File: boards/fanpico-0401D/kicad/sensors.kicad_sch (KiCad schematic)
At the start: 22 parts, among them J1 Floppy Power Connector, J16 Sensor1, J17 Sensor2, J18 LCD (SPI), J19 Serial Console (TTL), J2 I2C (OLED ALT), J3 I2C (OLED), J5 1-Wire, J6 QWIIC

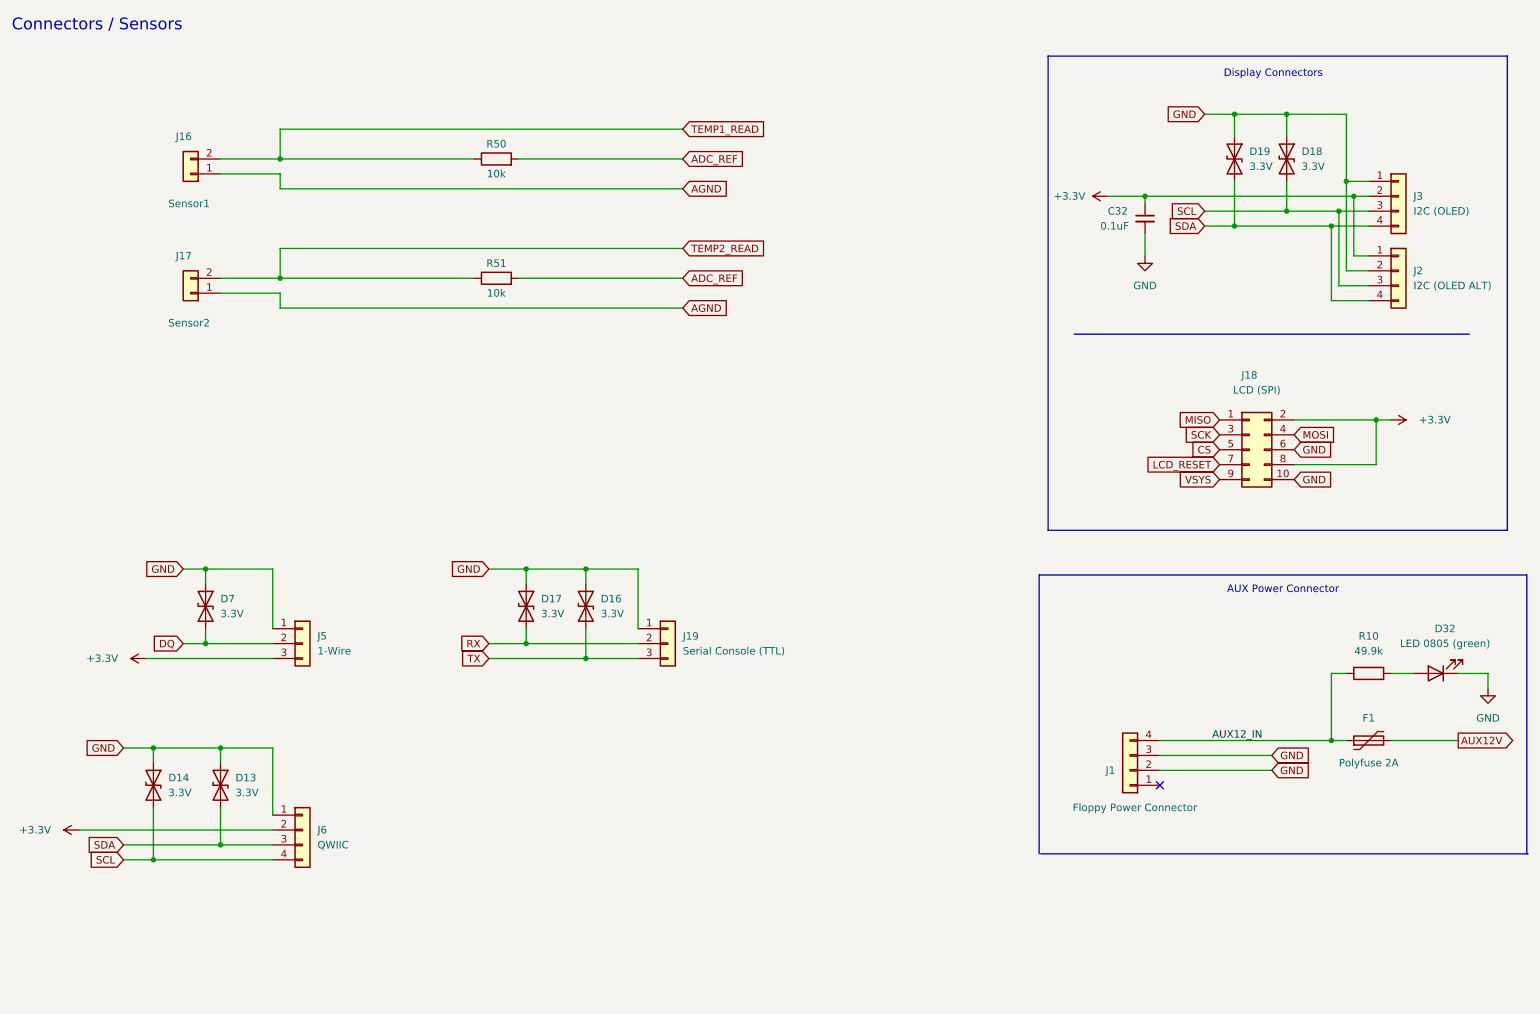
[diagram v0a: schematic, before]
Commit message: Add new 0401D v1.1 PCB (#116)
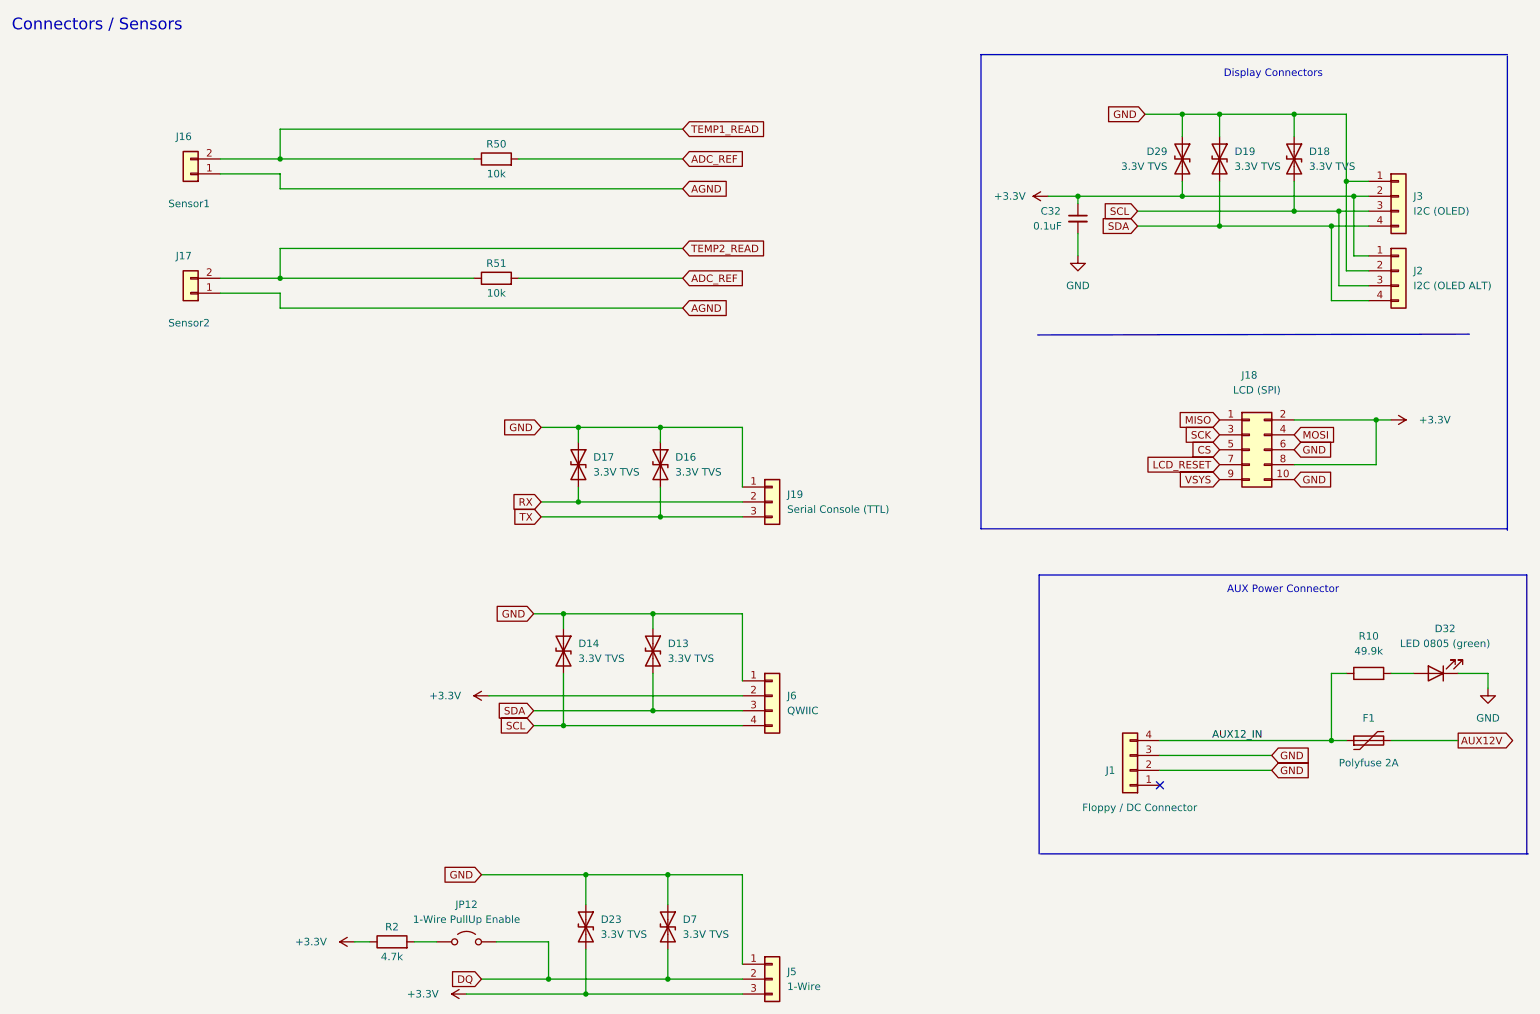
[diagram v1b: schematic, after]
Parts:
- added D23, D29: 3.3V TVS, Diode_SMD:D_SOD-323_HandSoldering, symbol Device:D_TVS
- added JP12: 1-Wire PullUp Enable, Connector_PinHeader_2.54mm:PinHeader_1x02_P2.54mm_Vertical, symbol Jumper:Jumper_2_Open
- added R2: 4.7k, Resistor_SMD:R_0603_1608Metric_Pad0.98x0.95mm_HandSolder, symbol Device:R
- D13, D14, D16, D17, D18, D19, D7: value 3.3V -> 3.3V TVS
- J1: value Floppy Power Connector -> Floppy / DC Connector
- J5: LCSC Part Number C1509679 -> C68305 or C5188443
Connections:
- net +3.3V: now also D23.2 (A2), D29.2 (A2), R2.1
- net DQ: now also JP12.2 (B)
- net GND: now also D23.1 (A1), D29.1 (A1)
- new net: JP12.1 (A), R2.2
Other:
- title: FanPico-0401D v1.0 -> FanPico-0401D v1.1
- moved on the sheet: C32, D13, D14, D16, D17, D18, D19, D7, J19, J5, J6
